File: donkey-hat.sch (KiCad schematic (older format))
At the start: 58 parts, among them J1 6-18V, J14 NEOPIXEL, J15 MPU-9250, J16 4, J17 5, J18 6, J19 7, J2 Raspberry_Pi_2_3, J24 3mm_Mount, J25 3mm_Mount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

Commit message: Added Regulator Bypass.
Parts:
- added J5: REG/BYPASS, Connector_PinHeader_2.54mm:PinHeader_1x03_P2.54mm_Vertical, symbol Connector_Generic:Conn_01x03
- D2, D3: Manufacturer (none) -> Worldsemi; Mfg Part # (none) -> WS2812B
- Q1: Manufacturer (none) -> International Rectifier; Mfg Part # (none) -> IRLML6402PbF
- RN1: Link https://www.aliexpress.com/item/200PCS-0603-2X4-220R-220-oh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 -> (none)
- U1: Manufacturer (none) -> ONsemi; Mfg Part # (none) -> CAT24C32
- U2: Manufacturer (none) -> NXP; Mfg Part # (none) -> PCA9685
- U3: Manufacturer (none) -> MPS; Mfg Part # (none) -> MPM3632C
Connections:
- net VIN_REG: now reaches C2.1, R15.1, U3.17 (VIN), U3.18 (VIN)
- net VIN_REG: now also J5.1 (Pin_1); no longer J1.2 (Pin_2)
- net REG: now reaches C4.1, Q1.3 (D), R12.1, R13.1, U3.8-9 (OUT)
- net REG: now also J5.3 (Pin_3)
- new net VIN: J1.2 (Pin_2), J5.2 (Pin_2)
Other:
- moved on the sheet: C2
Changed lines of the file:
@@
 F 4 "https://www.digikey.com.au/product-detail/en/nxp-usa-inc/PCA9685PW118/568-11925-1-ND/5221902" H 9800 3050 50  0001 C CNN "Link"
 F 5 "28-TSSOP" H 0   0   50  0001 C CNN "Package"
+F 6 "NXP" H 9800 3050 50  0001 C CNN "Manufacturer"
+F 7 "PCA9685" H 9800 3050 50  0001 C CNN "Mfg Part #"
 	1    9800 3050
 	1    0    0    -1
@@
 F 4 "https://www.digikey.com.au/product-detail/en/on-semiconductor/CAT24C32WI-GT3/CAT24C32WI-GT3CT-ND/1631159" H 1150 4800 50  0001 C CNN "Link"
 F 5 "8-SOIC" H 0   0   50  0001 C CNN "Package"
+F 6 "ONsemi" H 0   0   50  0001 C CNN "Manufacturer"
+F 7 "CAT24C32" H 0   0   50  0001 C CNN "Mfg Part #"
 	1    1150 4800
 	1    0    0    -1
@@
 F 2 "Resistor_SMD:R_Array_Convex_4x0603" V 5175 1500 50  0001 C CNN
 F 3 "~" H 4900 1500 50  0001 C CNN
-F 4 "https://www.aliexpress.com/item/200PCS-0603-2X4-220R-220-ohm-Marking-221-SMD-Network-Resistor-array-0603-8P4R-2-4P/32845505270.html?spm=2114.search0104.3.35.c74a11b9SNycSm&ws_ab_test=searchweb0_0,searchweb201602_2_10065_10068_10130_10547_319_317_10548_10696_453_10084_454_10083_10618_10307_537_536_10131_10132_10133_10059_10884_10887_100031_321_322_10103,searchweb201603_51,ppcSwitch_0&algo_expid=516fab08-5bb7-441c-804a-744d42f8303d-5&algo_pvid=516fab08-5bb7-441c-804a-744d42f8303d" V 4900 1500 50  0001 C CNN "Link"
+F 4 "" V 4900 1500 50  0001 C CNN "Link"
 F 5 "SMD" H 0   0   50  0001 C CNN "Package"
 	1    4900 1500
@@
 F 4 "https://www.digikey.com.au/product-detail/en/infineon-technologies/IRLML6401TRPBF/IRLML6401PBFCT-ND/812509" V 6650 5450 50  0001 C CNN "Link"
 F 5 "SOT-23" H 0   0   50  0001 C CNN "Package"
+F 6 "International Rectifier" H 0   0   50  0001 C CNN "Manufacturer"
+F 7 "IRLML6402PbF" H 0   0   50  0001 C CNN "Mfg Part #"
 	1    6650 5450
 	0    -1   -1   0
@@
 F 3 "https://cdn-shop.adafruit.com/datasheets/WS2812B.pdf" H 4550 6775 50  0001 L TNN
 F 4 "SMD" H 0   0   50  0001 C CNN "Package"
+F 5 "Worldsemi" H 0   0   50  0001 C CNN "Manufacturer"
+F 6 "WS2812B" H 0   0   50  0001 C CNN "Mfg Part #"
 	1    4450 7150
 	1    0    0    -1
@@
 F 3 "https://cdn-shop.adafruit.com/datasheets/WS2812B.pdf" H 5300 6775 50  0001 L TNN
 F 4 "SMD" H 0   0   50  0001 C CNN "Package"
+F 5 "Worldsemi" H 0   0   50  0001 C CNN "Manufacturer"
+F 6 "WS2812B" H 0   0   50  0001 C CNN "Mfg Part #"
 	1    5200 7150
 	1    0    0    -1
@@
 F 4 "https://www.digikey.com/product-detail/en/monolithic-power-systems-inc/MPM3632CGQV-Z/1589-1955-1-ND/9637668" H 4500 5450 50  0001 C CNN "Link"
 F 5 "20-QFN" H 0   0   50  0001 C CNN "Package"
+F 6 "MPS" H 0   0   50  0001 C CNN "Manufacturer"
+F 7 "MPM3632C" H 0   0   50  0001 C CNN "Mfg Part #"
 	1    4500 5450
 	1    0    0    -1
@@
 L power:GND #PWR0140
 U 1 1 5C0FC540
-P 3150 5600
-F 0 "#PWR0140" H 3150 5350 50  0001 C CNN
-F 1 "GND" H 3155 5427 50  0000 C CNN
-F 2 "" H 3150 5600 50  0001 C CNN
-F 3 "" H 3150 5600 50  0001 C CNN
-	1    3150 5600
+P 3200 5600
+F 0 "#PWR0140" H 3200 5350 50  0001 C CNN
+F 1 "GND" H 3205 5427 50  0000 C CNN
+F 2 "" H 3200 5600 50  0001 C CNN
+F 3 "" H 3200 5600 50  0001 C CNN
+	1    3200 5600
 	-1   0    0    -1
 $EndComp
@@
 L Device:C C2
 U 1 1 5C3DCB8C
-P 3150 5350
-F 0 "C2" H 3265 5396 50  0000 L CNN
-F 1 "10uF" H 3265 5305 50  0000 L CNN
-F 2 "Capacitor_SMD:C_1206_3216Metric_Pad1.42x1.75mm_HandSolder" H 3188 5200 50  0001 C CNN
-F 3 "~" H 3150 5350 50  0001 C CNN
-F 4 "1206" H 0   0   50  0001 C CNN "Package"
-	1    3150 5350
-	1    0    0    -1
-$EndComp
-Wire Wire Line
-	3150 5200 3150 5150
-Wire Wire Line
-	3150 5500 3150 5550
-Wire Wire Line
-	3150 5150 3000 5150
-Connection ~ 3150 5150
+P 3200 5350
+F 0 "C2" H 3315 5396 50  0000 L CNN
+F 1 "10uF" H 3315 5305 50  0000 L CNN
+F 2 "Capacitor_SMD:C_1206_3216Metric_Pad1.42x1.75mm_HandSolder" H 3238 5200 50  0001 C CNN
+F 3 "~" H 3200 5350 50  0001 C CNN
+F 4 "1206" H 50  0   50  0001 C CNN "Package"
+	1    3200 5350
+	1    0    0    -1
+$EndComp
+Wire Wire Line
+	3200 5500 3200 5550
+Wire Wire Line
+	3100 5150 3000 5150
 Wire Wire Line
 	3000 5250 3000 5550
 Wire Wire Line
-	3000 5550 3150 5550
-Connection ~ 3150 5550
-Wire Wire Line
-	3150 5550 3150 5600
+	3000 5550 3200 5550
+Connection ~ 3200 5550
+Wire Wire Line
+	3200 5550 3200 5600
 Wire Wire Line
 	5600 5350 5750 5350
@@
 	1    0    0    -1
 $EndComp
-Wire Wire Line
-	3150 5150 3550 5150
 Connection ~ 3750 5150
 Wire Wire Line
 	3550 5200 3550 5150
-Connection ~ 3550 5150
 Wire Wire Line
 	3550 5150 3750 5150
@@
 Text Notes 2600 4650 0    50   ~ 0
 6-20V 3A switch mode regulator\n
+Text Label 3550 5150 1    50   ~ 0
+VIN_REG
+Text Label 3200 6200 2    50   ~ 0
+VIN
+Wire Wire Line
+	3200 6100 2900 6100
+Wire Wire Line
+	3200 6200 2900 6200
+$Comp
+L Connector_Generic:Conn_01x03 J5
+U 1 1 5C1E72E1
+P 2700 6200
+F 0 "J5" H 2620 5875 50  0000 C CNN
+F 1 "REG/BYPASS" H 2620 5966 50  0000 C CNN
+F 2 "Connector_PinHeader_2.54mm:PinHeader_1x03_P2.54mm_Vertical" H 2700 6200 50  0001 C CNN
+F 3 "~" H 2700 6200 50  0001 C CNN
+	1    2700 6200
+	-1   0    0    1
+$EndComp
+Text Label 3100 5150 1    50   ~ 0
+VIN
+Text Label 3200 6300 2    50   ~ 0
+VIN_REG
+Wire Wire Line
+	3200 6300 2900 6300
+Wire Wire Line
+	3200 5200 3200 5150
+Wire Wire Line
+	3200 5150 3550 5150
+Connection ~ 3550 5150
+Text Label 6450 5350 2    50   ~ 0
+REG
+Text Label 3200 6100 2    50   ~ 0
+REG
 $EndSCHEMATC

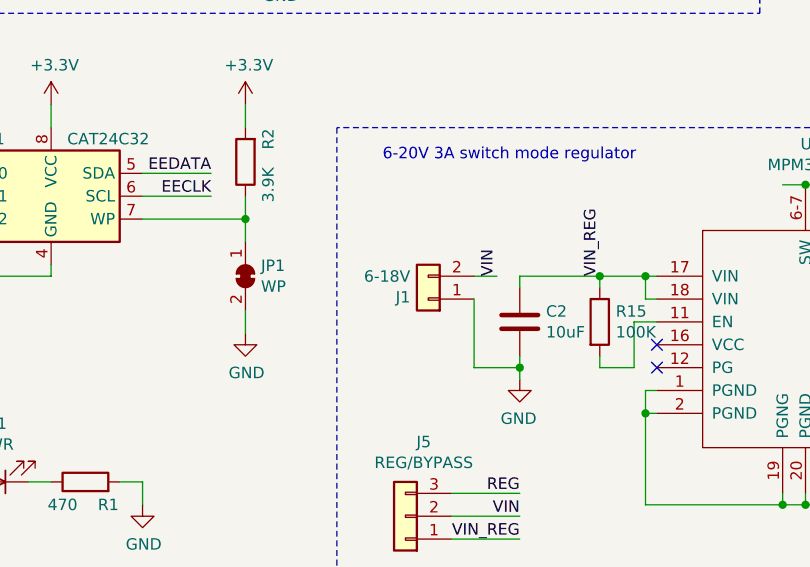
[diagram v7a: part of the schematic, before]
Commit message: Added logos and call outs.
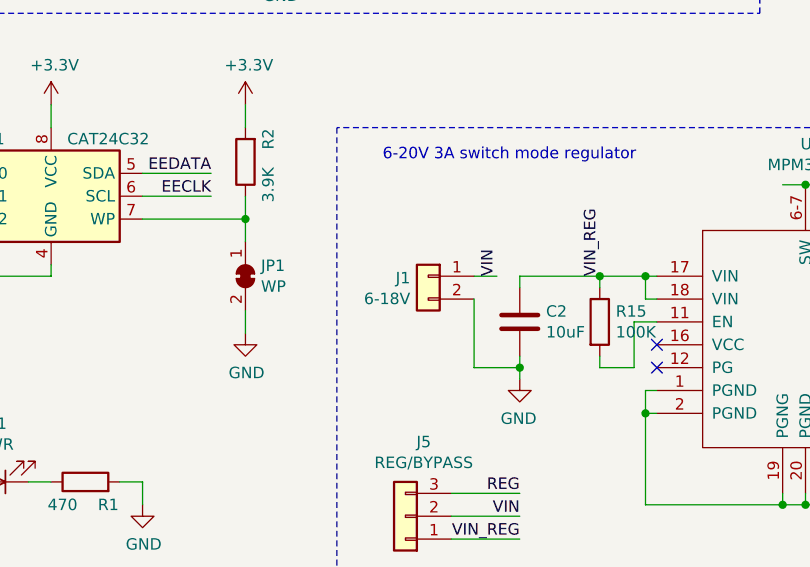
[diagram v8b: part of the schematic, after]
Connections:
- net GND: now also J1.2 (Pin_2); no longer J1.1 (Pin_1)
- net VIN: now also J1.1 (Pin_1); no longer J1.2 (Pin_2)
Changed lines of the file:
@@
 L Connector_Generic:Conn_01x02 J1
 U 1 1 5C20A2ED
-P 2800 5250
-F 0 "J1" H 2879 5242 50  0000 L CNN
-F 1 "6-18V" H 2879 5151 50  0000 L CNN
-F 2 "Connector_Phoenix_MC:PhoenixContact_MC_1,5_2-G-3.5_1x02_P3.50mm_Horizontal" H 2800 5250 50  0001 C CNN
-F 3 "~" H 2800 5250 50  0001 C CNN
-	1    2800 5250
-	-1   0    0    1
+P 2800 5150
+F 0 "J1" H 2879 5142 50  0000 L CNN
+F 1 "6-18V" H 2879 5051 50  0000 L CNN
+F 2 "Connector_Phoenix_MC:PhoenixContact_MC_1,5_2-G-3.5_1x02_P3.50mm_Horizontal" H 2800 5150 50  0001 C CNN
+F 3 "~" H 2800 5150 50  0001 C CNN
+	1    2800 5150
+	-1   0    0    -1
 $EndComp
 $Comp
@@
 	3100 5150 3000 5150
 Wire Wire Line
-	3000 5250 3000 5550
-Wire Wire Line
 	3000 5550 3200 5550
 Connection ~ 3200 5550
@@
 Text Label 3200 6100 2    50   ~ 0
 REG
+Wire Wire Line
+	3000 5250 3000 5550
 $EndSCHEMATC
